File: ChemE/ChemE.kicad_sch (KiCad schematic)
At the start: 12 parts, among them IC1 LF353P, J1 Circuit Battery, Q1 MTP3055E, U1 LM393N

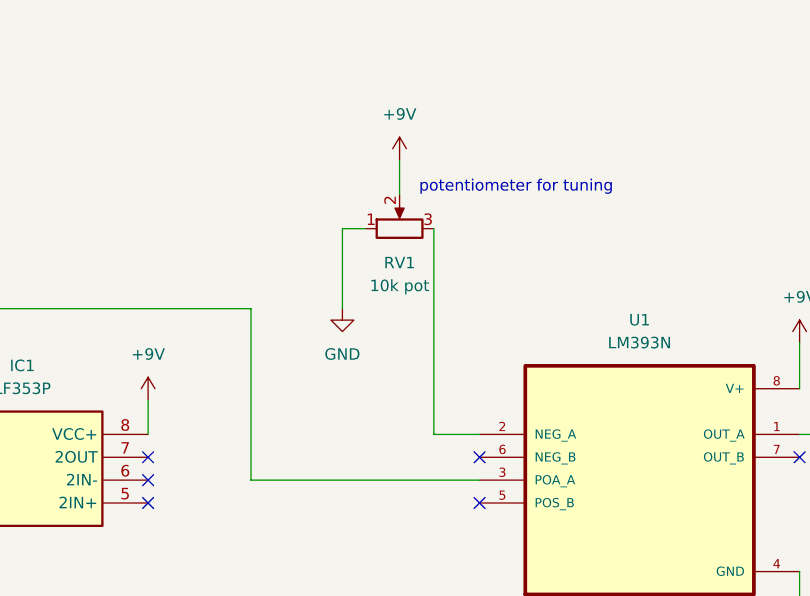
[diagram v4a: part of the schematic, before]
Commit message: redid pot with correct wiring
https://www.piher.net/wp-content/uploads/PIHER_PT-15_PTC-15.pdf

also made prod. should be good to order.
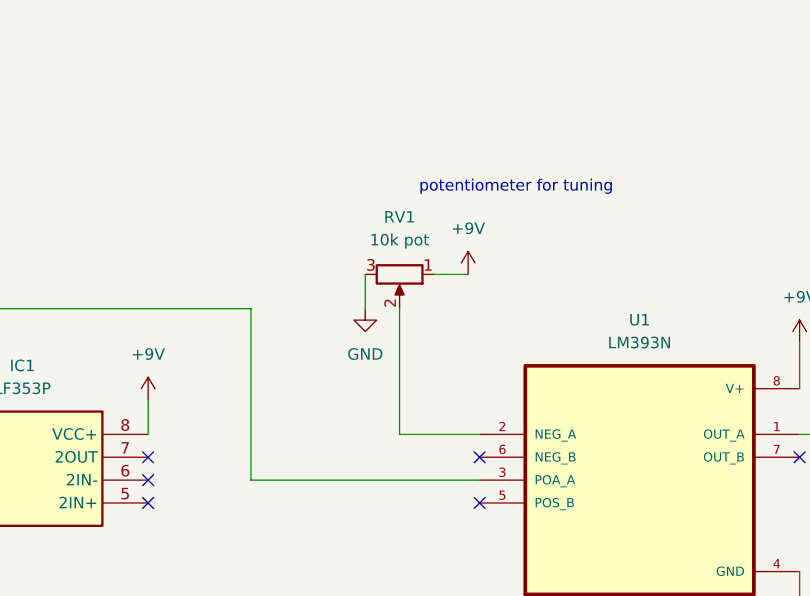
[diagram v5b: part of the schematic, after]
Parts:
- RV1: footprint Potentiometer_THT:Potentiometer_ACP_CA9-H5_Horizontal -> Potentiometer_THT:Potentiometer_Piher_PT-6-H_Horizontal
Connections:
- net +9V: now also RV1.1; no longer RV1.2
- net GND: now also RV1.3; no longer RV1.1
- net at U1.2 (NEG_A): now also RV1.2; no longer RV1.3
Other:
- moved on the sheet: RV1
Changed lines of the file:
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@@
 	(wire
 		(pts
-			(xy 158.75 41.91) (xy 158.75 50.8)
-		)
-		(stroke
-			(width 0)
-			(type default)
-		)
-	)
-	(wire
-		(pts
-			(xy 168.91 41.91) (xy 168.91 64.77)
+			(xy 168.91 46.99) (xy 172.72 46.99)
 		)
 		(stroke
@@
 	(wire
 		(pts
-			(xy 165.1 34.29) (xy 165.1 38.1)
-		)
-		(stroke
-			(width 0)
-			(type default)
-		)
-	)
-	(wire
-		(pts
 			(xy 85.09 27.94) (xy 88.9 27.94)
 		)
@@
 	(wire
 		(pts
-			(xy 168.91 64.77) (xy 173.99 64.77)
-		)
-		(stroke
-			(width 0)
-			(type default)
-		)
-	)
-	(wire
-		(pts
 			(xy 250.19 34.29) (xy 251.46 34.29)
 		)
@@
 	(wire
 		(pts
-			(xy 161.29 41.91) (xy 158.75 41.91)
-		)
-		(stroke
-			(width 0)
-			(type default)
-		)
-	)
-	(wire
-		(pts
 			(xy 261.62 45.72) (xy 261.62 55.88)
 		)
@@
 	(wire
 		(pts
+			(xy 161.29 46.99) (xy 161.29 50.8)
+		)
+		(stroke
+			(width 0)
+			(type default)
+		)
+	)
+	(wire
+		(pts
 			(xy 255.27 72.39) (xy 255.27 82.55)
 		)
@@
 	(wire
 		(pts
+			(xy 165.1 64.77) (xy 173.99 64.77)
+		)
+		(stroke
+			(width 0)
+			(type default)
+		)
+	)
+	(wire
+		(pts
 			(xy 88.9 59.69) (xy 88.9 50.8)
+		)
+		(stroke
+			(width 0)
+			(type default)
+		)
+	)
+	(wire
+		(pts
+			(xy 165.1 50.8) (xy 165.1 64.77)
 		)
 		(stroke
@@
 	(symbol
 		(lib_id "power:+9V")
-		(at 165.1 34.29 0)
+		(at 172.72 46.99 0)
 		(unit 1)
 		(exclude_from_sim no)
@@
 		(fields_autoplaced yes)
 		(property "Reference" "#PWR08"
-			(at 165.1 38.1 0)
+			(at 172.72 50.8 0)
 			(effects
 				(font
@@
 		)
 		(property "Value" "+9V"
-			(at 165.1 29.21 0)
+			(at 172.72 41.91 0)
 			(effects
 				(font
@@
 		)
 		(property "Footprint" ""
-			(at 165.1 34.29 0)
+			(at 172.72 46.99 0)
 			(effects
 				(font
@@
 		)
 		(property "Datasheet" ""
-			(at 165.1 34.29 0)
+			(at 172.72 46.99 0)
 			(effects
 				(font
@@
 		)
 		(property "Description" "Power symbol creates a global label with name \"+9V\""
-			(at 165.1 34.29 0)
+			(at 172.72 46.99 0)
 			(effects
 				(font
@@
 	(symbol
 		(lib_id "Device:R_Potentiometer")
-		(at 165.1 41.91 90)
+		(at 165.1 46.99 270)
 		(unit 1)
 		(exclude_from_sim no)
@@
 		(fields_autoplaced yes)
 		(property "Reference" "RV1"
-			(at 165.1 45.72 90)
+			(at 165.1 40.64 90)
 			(effects
 				(font
@@
 		)
 		(property "Value" "10k pot"
-			(at 165.1 48.26 90)
-			(effects
-				(font
-					(size 1.27 1.27)
-				)
-			)
-		)
-		(property "Footprint" "Potentiometer_THT:Potentiometer_ACP_CA9-H5_Horizontal"
-			(at 165.1 41.91 0)
+			(at 165.1 43.18 90)
+			(effects
+				(font
+					(size 1.27 1.27)
+				)
+			)
+		)
+		(property "Footprint" "Potentiometer_THT:Potentiometer_Piher_PT-6-H_Horizontal"
+			(at 165.1 46.99 0)
 			(effects
 				(font
@@
 		)
 		(property "Datasheet" "~"
-			(at 165.1 41.91 0)
+			(at 165.1 46.99 0)
 			(effects
 				(font
@@
 		)
 		(property "Description" "Potentiometer"
-			(at 165.1 41.91 0)
+			(at 165.1 46.99 0)
 			(effects
 				(font
@@
 	(symbol
 		(lib_id "power:GND")
-		(at 158.75 50.8 0)
+		(at 161.29 50.8 0)
 		(unit 1)
 		(exclude_from_sim no)
@@
 		(fields_autoplaced yes)
 		(property "Reference" "#PWR09"
-			(at 158.75 57.15 0)
+			(at 161.29 57.15 0)
 			(effects
 				(font
@@
 		)
 		(property "Value" "GND"
-			(at 158.75 55.88 0)
+			(at 161.29 55.88 0)
 			(effects
 				(font
@@
 		)
 		(property "Footprint" ""
-			(at 158.75 50.8 0)
+			(at 161.29 50.8 0)
 			(effects
 				(font
@@
 		)
 		(property "Datasheet" ""
-			(at 158.75 50.8 0)
+			(at 161.29 50.8 0)
 			(effects
 				(font
@@
 		)
 		(property "Description" "Power symbol creates a global label with name \"GND\" , ground"
-			(at 158.75 50.8 0)
-			(effects
-				(font
+			(at 161.29 50.8 0)
+			(effects
+				(font

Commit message: updated design w/ new components and footprints
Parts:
- removed Q1: MTP3055E, Package_TO_SOT_THT:TO-247-3_Vertical, symbol Simulation_SPICE:NMOS
- removed RV1: 10k pot, Potentiometer_THT:Potentiometer_Piher_PT-6-H_Horizontal, symbol Device:R_Potentiometer
- added Q2: IRLZ44NPBF, mosfet:TO254P469X1042X1967-3P, symbol mosfet:IRLZ44NPBF
- added R4: 3296W-1-103LF, step:POT_3296W, symbol step:3296W-1-103LF
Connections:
- net +9V: now also R4.1
- net GND: now also Q2.3 (S), R4.3
- net at D2.2 (A), motor1.2 (Pin_2): now also Q2.2 (D)
- net at R2.2, R3.2: now also Q2.1 (G)
- net at U1.2 (NEG_A): now also R4.2
